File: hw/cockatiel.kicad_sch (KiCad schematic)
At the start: 40 parts, among them J1 Programmer, J10 MIC_N_BYP, J11 MIC_P_SEL, J12 MIC_N_SEL, J13 Cox Box Mic In, J14 Cox Box Mic Out, J15 Mic Out, J16 Headset/Mic In, J3 DEBUG_UART, J4 RESET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

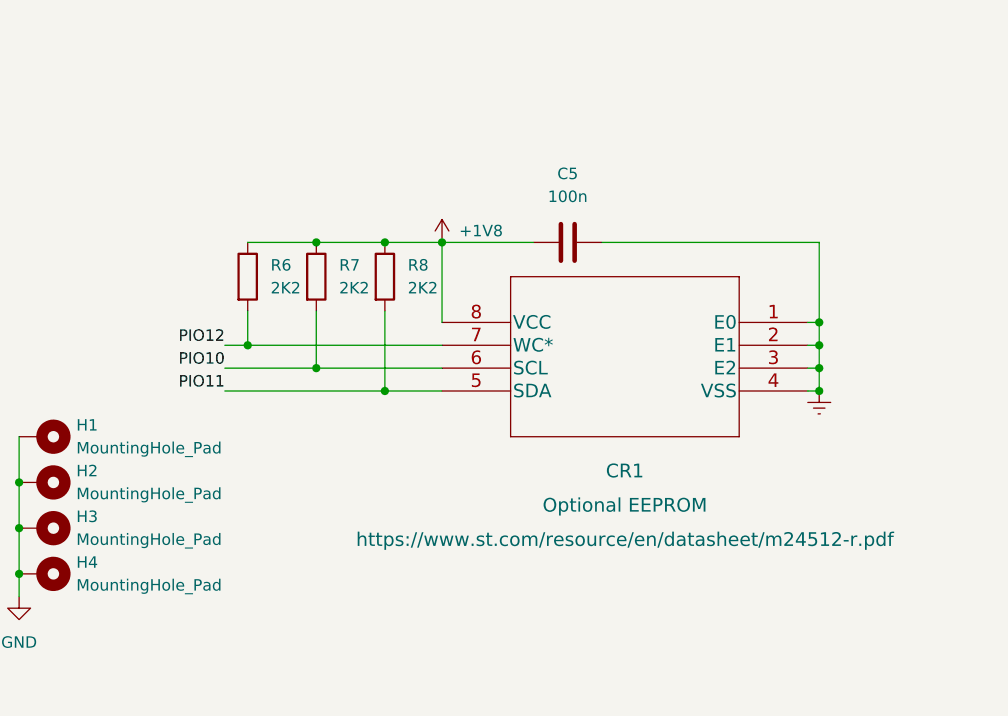
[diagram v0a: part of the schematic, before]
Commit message: Remove the 'optional' EEPROM
The module already has EEPROM fitted. Removing this simplifies board
layout and size, which will come in handy in the future.
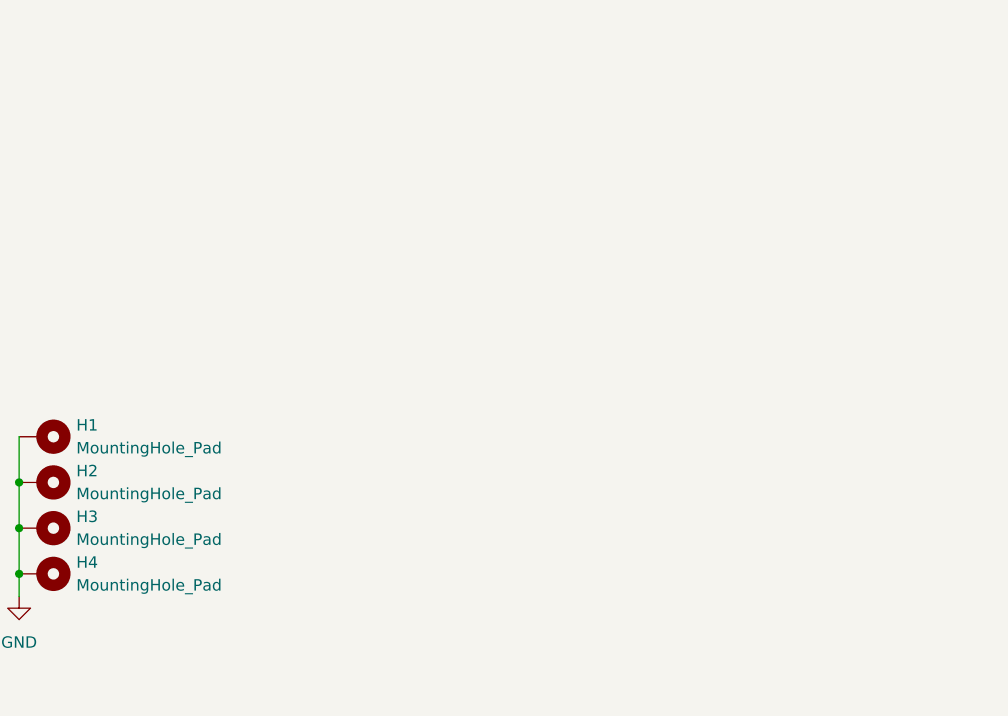
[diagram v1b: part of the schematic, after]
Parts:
- removed C5: 100n, Capacitor_SMD:C_0805_2012Metric_Pad1.18x1.45mm_HandSolder, symbol Device:C
- removed CR1: Optional EEPROM, st:M24512-RMN6P, symbol 2022-08-27_17-15-02:M24512-RMN6P
- removed R6, R7, R8: 2K2, Resistor_SMD:R_0805_2012Metric_Pad1.20x1.40mm_HandSolder, symbol Device:R
